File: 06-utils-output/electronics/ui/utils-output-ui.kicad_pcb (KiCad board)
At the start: 2 copper layers, 58 x 110 mm, 35 parts, among them J1 Conn_02x03_Odd_Even, J2 Conn_02x04_Odd_Even, J3 Conn_02x02_Odd_Even, J4 Conn_01x02, J5 Conn_01x06, J6 Conn_02x05_Odd_Even, Q1 2N3904

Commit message: Utils+output PCB connectors positions checked
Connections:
- J5 pad 3: OUTPUT_OUT_DEFAULT -> unconnected-(J5-Pin_3-Pad3)
- J_MAIN_OUT1 pad TN: OUTPUT_OUT_DEFAULT -> OUTPUT_OUT
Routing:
- net OUTPUT_OUT_DEFAULT: track 136.0 -> 0.00 mm
- net OUTPUT_OUT: track 27.2 -> 34.5 mm
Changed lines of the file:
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@@
 	(net 16 "LFO_RATE")
 	(net 17 "unconnected-(J3-Pin_4-Pad4)")
-	(net 18 "OUTPUT_OUT_DEFAULT")
+	(net 18 "unconnected-(J5-Pin_3-Pad3)")
 	(net 19 "CRUSH_IN_DEFAULT")
 	(net 20 "CRUSH_OUT_DEFAULT")
@@
 			(layers "*.Cu" "*.Mask")
 			(remove_unused_layers no)
-			(net 18 "OUTPUT_OUT_DEFAULT")
+			(net 18 "unconnected-(J5-Pin_3-Pad3)")
 			(pinfunction "Pin_3")
-			(pintype "passive")
+			(pintype "passive+no_connect")
 		)
 		(pad "4" thru_hole circle
@@
 			(layers "*.Cu" "*.Mask")
 			(remove_unused_layers no)
-			(net 18 "OUTPUT_OUT_DEFAULT")
+			(net 34 "OUTPUT_OUT")
 			(pintype "passive")
 		)
@@
 	)
 	(segment
-		(start 139.875 53.652)
-		(end 138.58 52.357)
-		(width 0.508)
-		(layer "F.Cu")
-		(net 18)
-	)
-	(segment
-		(start 142.161 143.06)
-		(end 142.161 63.558)
-		(width 0.508)
-		(layer "F.Cu")
-		(net 18)
-	)
-	(segment
-		(start 144.447 61.272)
-		(end 144.447 55.684)
-		(width 0.508)
-		(layer "F.Cu")
-		(net 18)
-	)
-	(segment
-		(start 169 135.62)
-		(end 166.492 135.62)
-		(width 0.508)
-		(layer "F.Cu")
-		(net 18)
-	)
-	(segment
-		(start 164.767 142.298)
-		(end 158.29 148.775)
-		(width 0.508)
-		(layer "F.Cu")
-		(net 18)
-	)
-	(segment
-		(start 142.415 53.652)
-		(end 139.875 53.652)
-		(width 0.508)
-		(layer "F.Cu")
-		(net 18)
-	)
-	(segment
-		(start 144.447 55.684)
-		(end 142.415 53.652)
-		(width 0.508)
-		(layer "F.Cu")
-		(net 18)
-	)
-	(segment
-		(start 164.767 137.345)
-		(end 164.767 142.298)
-		(width 0.508)
-		(layer "F.Cu")
-		(net 18)
-	)
-	(segment
-		(start 142.161 63.558)
-		(end 144.447 61.272)
-		(width 0.508)
-		(layer "F.Cu")
-		(net 18)
-	)
-	(segment
-		(start 138.58 52.357)
-		(end 138.58 49.5)
-		(width 0.508)
-		(layer "F.Cu")
-		(net 18)
-	)
-	(segment
-		(start 147.876 148.775)
-		(end 142.161 143.06)
-		(width 0.508)
-		(layer "F.Cu")
-		(net 18)
-	)
-	(segment
-		(start 166.492 135.62)
-		(end 164.767 137.345)
-		(width 0.508)
-		(layer "F.Cu")
-		(net 18)
-	)
-	(segment
-		(start 158.29 148.775)
-		(end 147.876 148.775)
-		(width 0.508)
-		(layer "F.Cu")
-		(net 18)
-	)
-	(segment
 		(start 137 111.62)
 		(end 135.501 111.62)
@@
 	)
 	(segment
-		(start 145.463 54.668)
-		(end 141.12 50.325)
+		(start 157.528 147.505)
+		(end 148.257 147.505)
 		(width 0.508)
 		(layer "F.Cu")
@@
 	)
 	(segment
-		(start 163.751 113.977)
-		(end 163.751 141.282)
+		(start 143.177 142.425)
+		(end 143.177 64.32)
 		(width 0.508)
 		(layer "F.Cu")
@@
 	)
 	(segment
-		(start 148.257 147.505)
-		(end 143.177 142.425)
+		(start 141.12 50.325)
+		(end 141.12 49.5)
 		(width 0.508)
 		(layer "F.Cu")
@@
 	)
 	(segment
-		(start 166.108 111.62)
-		(end 163.751 113.977)
+		(start 169 111.62)
+		(end 166.108 111.62)
 		(width 0.508)
 		(layer "F.Cu")
@@
 	)
 	(segment
-		(start 141.12 50.325)
-		(end 141.12 49.5)
+		(start 163.751 113.977)
+		(end 163.751 141.282)
 		(width 0.508)
 		(layer "F.Cu")
@@
 	)
 	(segment
-		(start 163.751 141.282)
-		(end 157.528 147.505)
+		(start 148.257 147.505)
+		(end 143.177 142.425)
 		(width 0.508)
 		(layer "F.Cu")
@@
 	)
 	(segment
-		(start 145.463 62.034)
-		(end 145.463 54.668)
+		(start 143.177 64.32)
+		(end 145.463 62.034)
 		(width 0.508)
 		(layer "F.Cu")
@@
 	)
 	(segment
-		(start 157.528 147.505)
-		(end 148.257 147.505)
+		(start 145.463 54.668)
+		(end 141.12 50.325)
 		(width 0.508)
 		(layer "F.Cu")
@@
 	)
 	(segment
-		(start 143.177 64.32)
-		(end 145.463 62.034)
+		(start 166.108 111.62)
+		(end 163.751 113.977)
 		(width 0.508)
 		(layer "F.Cu")
@@
 	)
 	(segment
-		(start 143.177 142.425)
-		(end 143.177 64.32)
+		(start 163.751 141.282)
+		(end 157.528 147.505)
 		(width 0.508)
 		(layer "F.Cu")
@@
 	)
 	(segment
-		(start 169 111.62)
-		(end 166.108 111.62)
+		(start 145.463 62.034)
+		(end 145.463 54.668)
 		(width 0.508)
 		(layer "F.Cu")
@@
 	)
 	(segment
+		(start 176.2732 128.4804)
+		(end 176.2732 135.694)
+		(width 0.508)
+		(layer "F.Cu")
+		(net 34)
+	)
+	(segment
 		(start 173.3812 143.92)
 		(end 169 143.92)
@@
 	)
 	(segment
-		(start 176.2732 128.4804)
+		(start 169 135.62)
+		(end 176.1992 135.62)
+		(width 0.508)
+		(layer "F.Cu")
+		(net 34)
+	)
+	(segment
+		(start 176.2732 135.694)
 		(end 176.2732 141.028)
 		(width 0.508)
@@
 		(width 0.508)
 		(layer "F.Cu")
+		(net 34)
+	)
+	(segment
+		(start 176.1992 135.62)
+		(end 176.2732 135.694)
+		(width 0.508)
+		(layer "F.Cu")

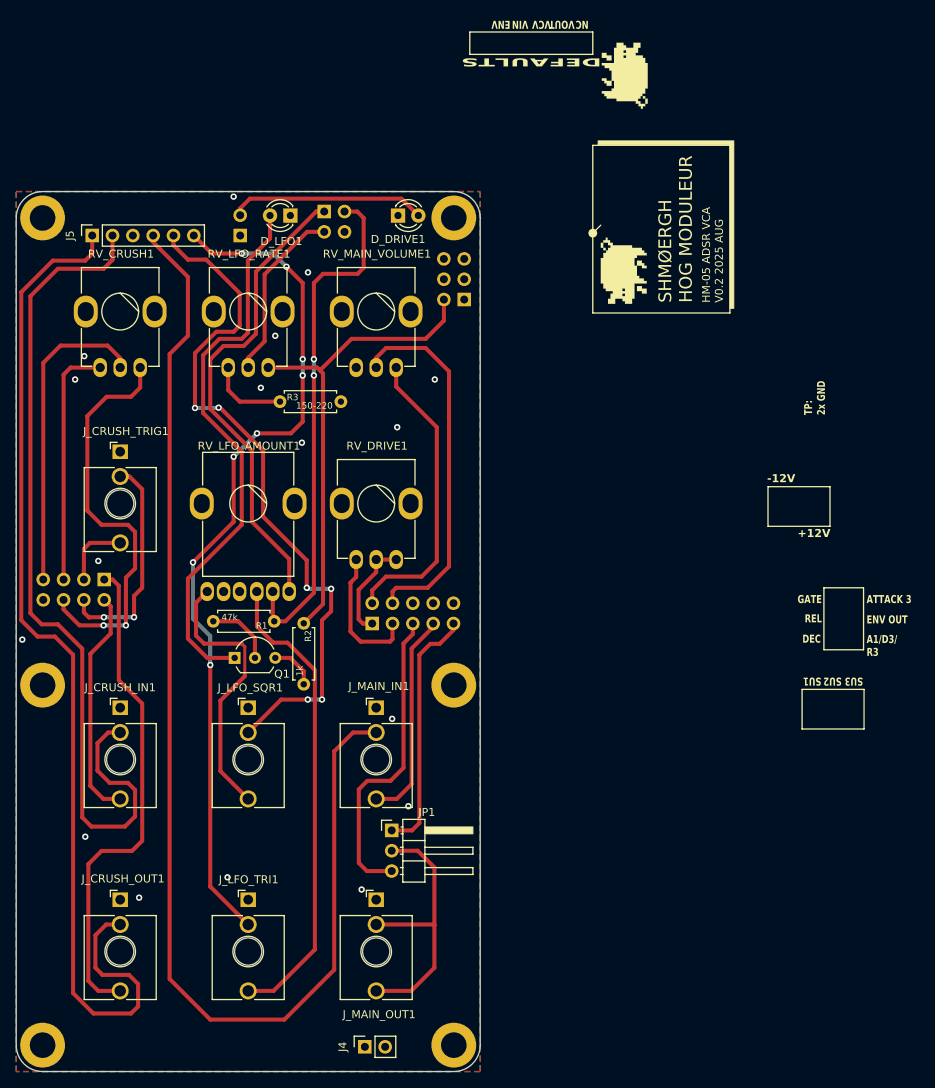
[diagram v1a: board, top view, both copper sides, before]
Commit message: Utils+output UI PCB done
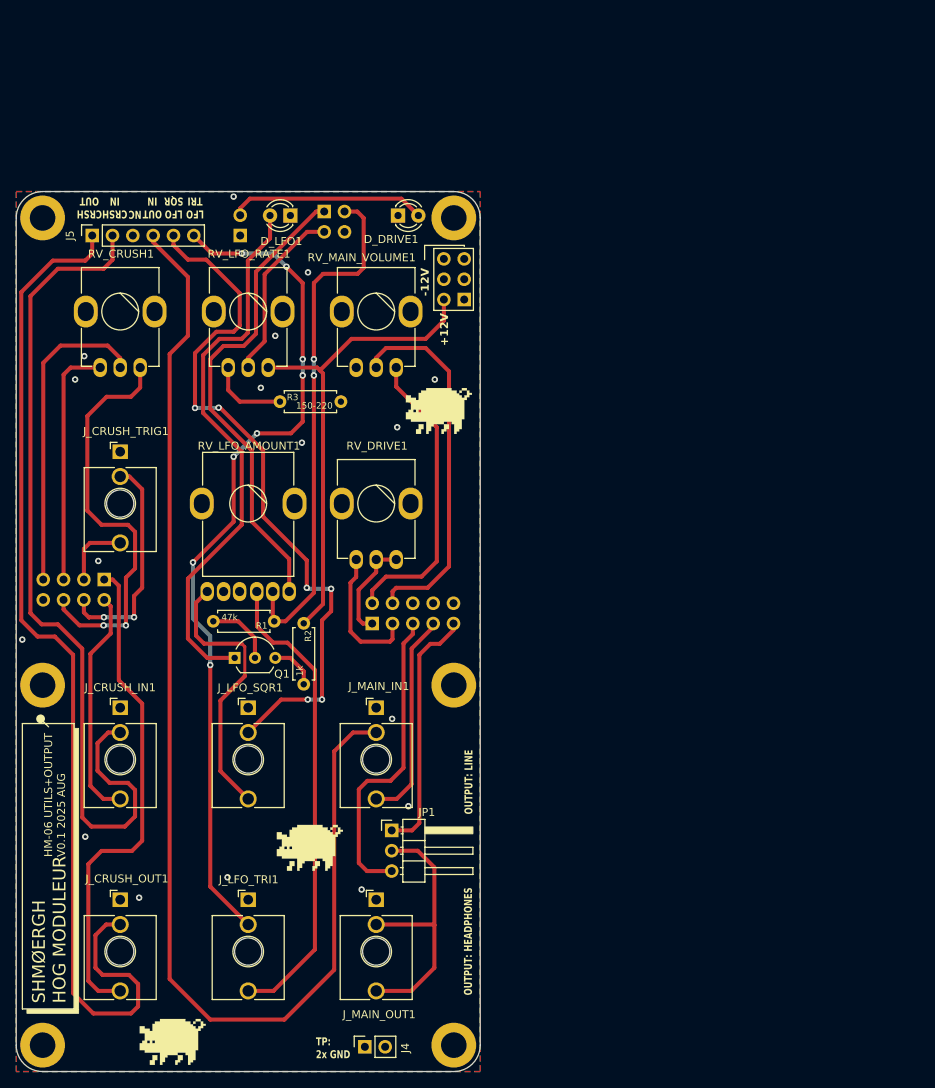
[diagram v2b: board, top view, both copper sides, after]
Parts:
- removed the G*** at (199.9, 53.9)
- removed the G*** at (197.8, 73.3)
- added G***: LOGO, Shmoergh_Logo:Gyeszno, F.Cu at (143.6, 150.3)
- added G***: LOGO, Shmoergh_Logo:Gyeszno, F.Cu at (160.7, 126.0)
- moved G*** 47.9 mm to (176.8, 71.4), turned to 0 degrees
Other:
- board text added: "CRSH IN"
- board text added: "CRSH OUT"
- board text added: "HM-06 UTILS+OUTPUT V0.1 2025 AUG"
- board text added: "LFO SQR"
- board text added: "LFO TRI"
- board text added: "OUT IN"
- board text added: "OUTPUT: HEADPHONES"
- board text added: "OUTPUT: LINE"
- board text removed: "A1/D3/ R3"
- board text removed: "ATTACK 3"
- board text removed: "DEC"
- board text removed: "DEFAULTS"
- board text removed: "ENV"
- board text removed: "ENV OUT"
- board text removed: "GATE"
- board text removed: "HM-05 ADSR VCA V0.2 2025 AUG"
- board text removed: "REL"
- board text removed: "SU1"
- board text removed: "SU2"
- board text removed: "SU3"
- board text removed: "VCV"
- board text removed: "VIN"
- board text removed: "VOUT"

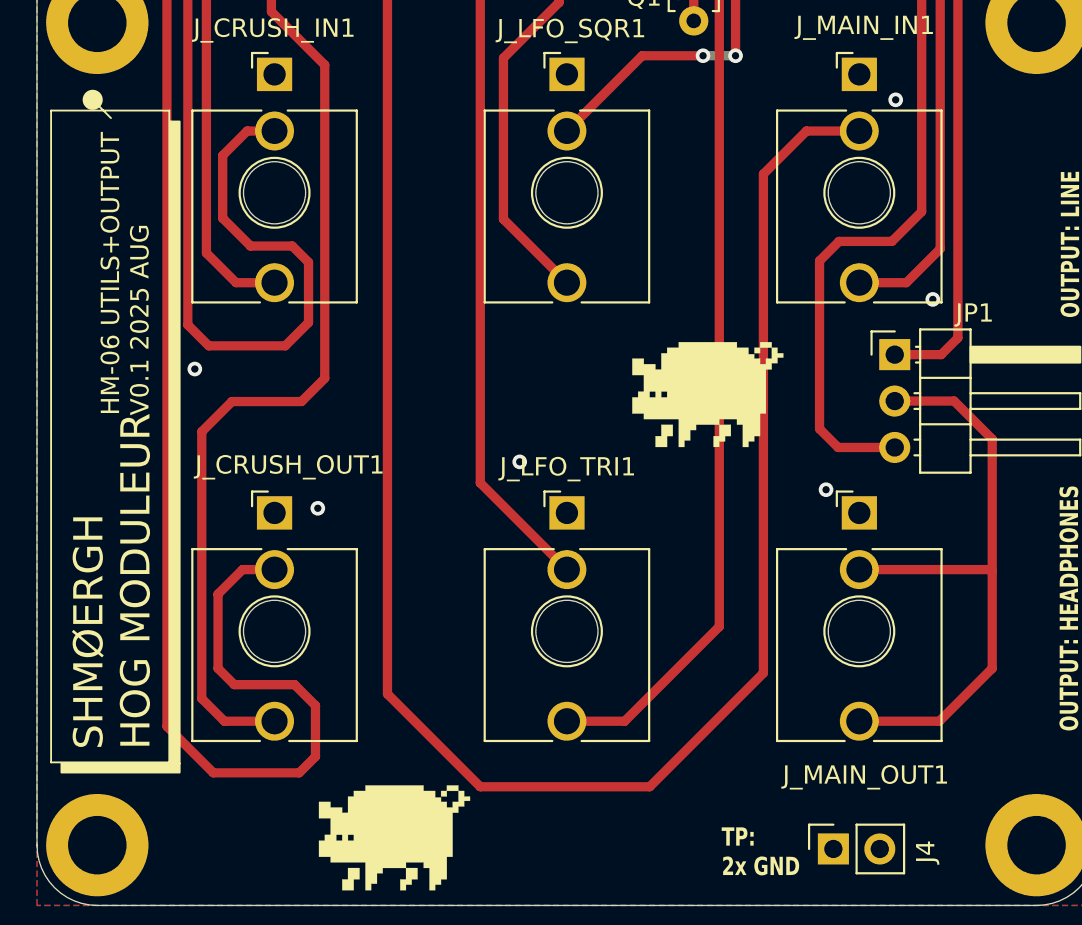
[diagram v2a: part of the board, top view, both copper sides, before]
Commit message: Added production files for Utils+output
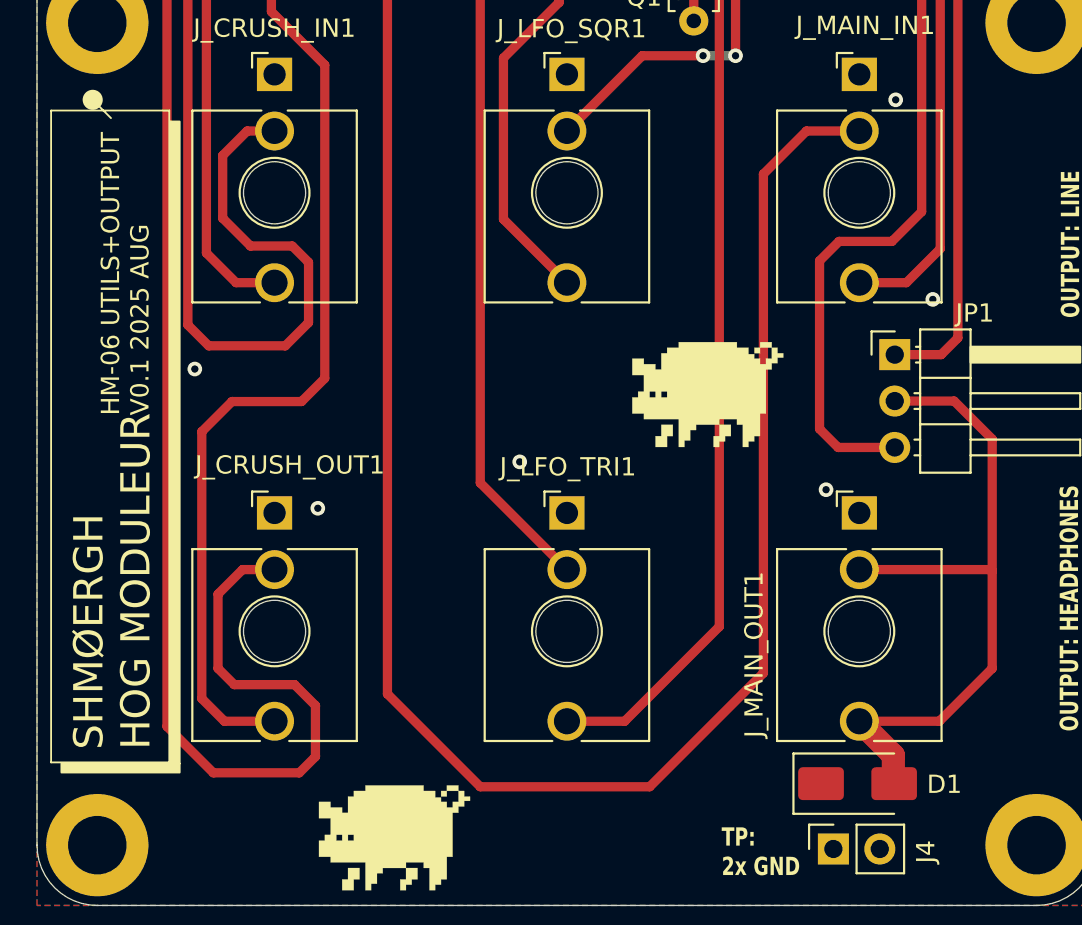
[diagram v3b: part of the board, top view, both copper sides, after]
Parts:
- added D1: SMAJ5.0CA, Diode_SMD:D_SMA, F.Cu at (168.9, 147.3)
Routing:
- net OUTPUT_OUT: track 34.5 -> 38.7 mm
